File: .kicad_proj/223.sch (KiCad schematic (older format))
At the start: 5 parts, among them U1 ATmega328-PU

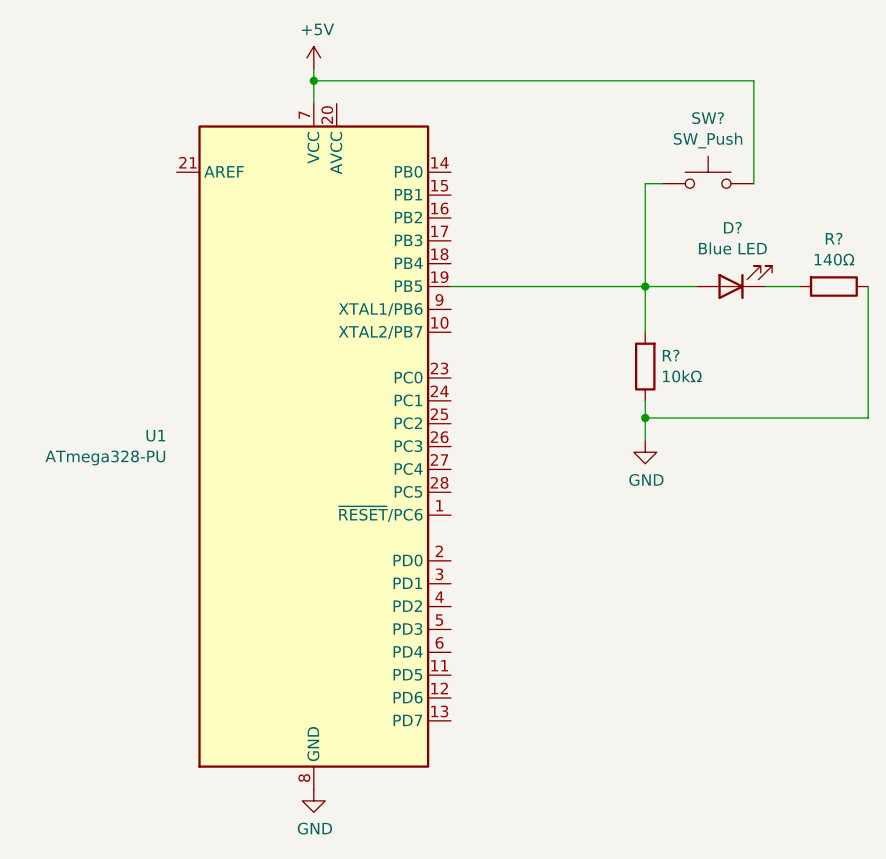
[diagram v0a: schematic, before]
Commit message: Finish 2.2.3, change R values in 2.2.7, change 3-state switch component in 2.2.2
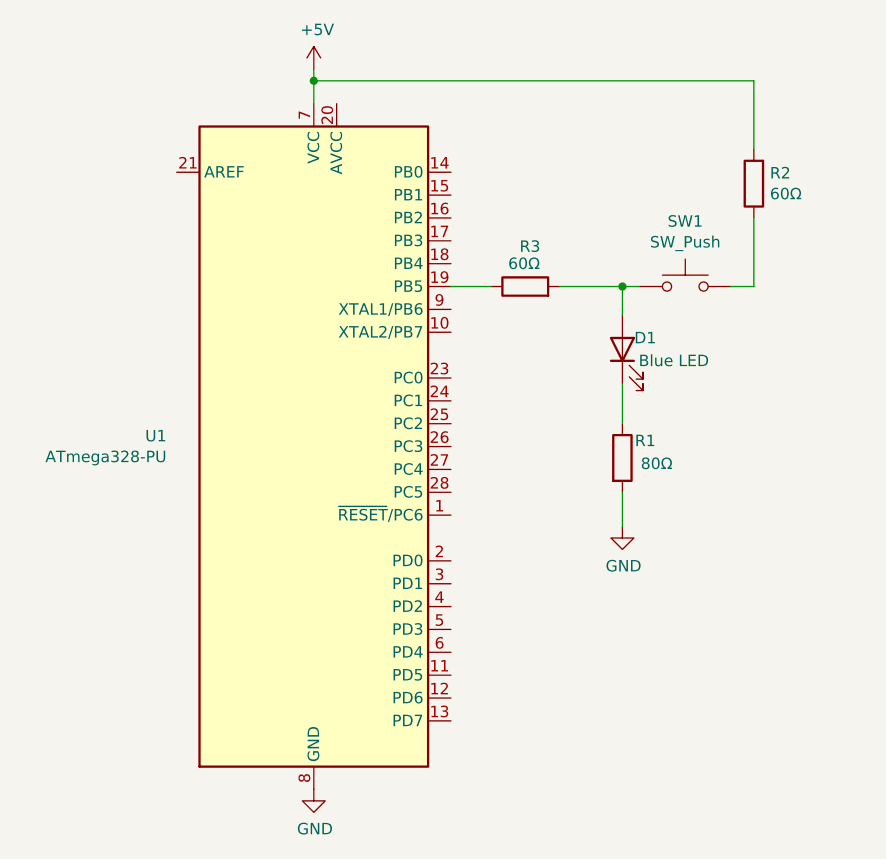
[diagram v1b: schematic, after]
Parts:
- added R3: 60Ω, symbol Device:R
- R1: renamed from R?; value 140Ω -> 80Ω
- R2: renamed from R?; value 10kΩ -> 60Ω
- gave numbers to parts that had none: 2
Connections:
- net +5V: now also R2.2; no longer SW1.2
- net GND: now also R1.2; no longer R1.1, R2.1
- net at D1.2 (A), SW1.1: now also R3.2; no longer R2.2, U1.19 (PB5)
- net at D1.1 (K): now also R1.1; no longer R1.2
- new net: R3.1, U1.19 (PB5)
- new net: R2.1, SW1.2
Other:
- moved on the sheet: D1, R1, R2, SW1
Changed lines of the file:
@@
 L Device:R R?
 U 1 1 607CCF46
-P 6850 3075
+P 5925 3825
 AR Path="/607CCF46" Ref="R?"  Part="1"
-AR Path="/607B21AE/607CCF46" Ref="R?"  Part="1"
-F 0 "R?" V 6643 3075 50  0000 C CNN
-F 1 "140Ω" V 6734 3075 50  0000 C CNN
-F 2 "" V 6780 3075 50  0001 C CNN
-F 3 "~" H 6850 3075 50  0001 C CNN
-	1    6850 3075
-	0    1    1    0
+AR Path="/607B21AE/607CCF46" Ref="R1"  Part="1"
+F 0 "R1" H 6025 3900 50  0000 C CNN
+F 1 "80Ω" H 6075 3800 50  0000 C CNN
+F 2 "" V 5855 3825 50  0001 C CNN
+F 3 "~" H 5925 3825 50  0001 C CNN
+	1    5925 3825
+	1    0    0    -1
 $EndComp
 $Comp
 L Device:LED D?
 U 1 1 607CCF4C
-P 6400 3075
+P 5925 3350
 AR Path="/607CCF4C" Ref="D?"  Part="1"
-AR Path="/607B21AE/607CCF4C" Ref="D?"  Part="1"
-F 0 "D?" H 6393 2820 50  0000 C CNN
-F 1 "Blue LED" H 6393 2911 50  0000 C CNN
-F 2 "" H 6400 3075 50  0001 C CNN
-F 3 "~" H 6400 3075 50  0001 C CNN
-	1    6400 3075
-	-1   0    0    1
+AR Path="/607B21AE/607CCF4C" Ref="D1"  Part="1"
+F 0 "D1" V 5975 3250 50  0000 C CNN
+F 1 "Blue LED" V 5875 3125 50  0000 C CNN
+F 2 "" H 5925 3350 50  0001 C CNN
+F 3 "~" H 5925 3350 50  0001 C CNN
+	1    5925 3350
+	0    -1   -1   0
 $EndComp
 $Comp
 L power:GND #PWR?
 U 1 1 607CCF52
-P 6025 3750
+P 5925 4125
 AR Path="/607CCF52" Ref="#PWR?"  Part="1"
 AR Path="/607B21AE/607CCF52" Ref="#PWR?"  Part="1"
-F 0 "#PWR?" H 6025 3500 50  0001 C CNN
-F 1 "GND" H 6030 3577 50  0000 C CNN
-F 2 "" H 6025 3750 50  0001 C CNN
-F 3 "" H 6025 3750 50  0001 C CNN
-	1    6025 3750
+F 0 "#PWR?" H 5925 3875 50  0001 C CNN
+F 1 "GND" H 5930 3952 50  0000 C CNN
+F 2 "" H 5925 4125 50  0001 C CNN
+F 3 "" H 5925 4125 50  0001 C CNN
+	1    5925 4125
 	1    0    0    -1
 $EndComp
@@
 L Switch:SW_Push SW?
 U 1 1 607CCF58
-P 6300 2625
+P 6200 3075
 AR Path="/607CCF58" Ref="SW?"  Part="1"
-AR Path="/607B21AE/607CCF58" Ref="SW?"  Part="1"
-F 0 "SW?" H 6300 2910 50  0000 C CNN
-F 1 "SW_Push" H 6300 2819 50  0000 C CNN
-F 2 "" H 6300 2825 50  0001 C CNN
-F 3 "~" H 6300 2825 50  0001 C CNN
-	1    6300 2625
+AR Path="/607B21AE/607CCF58" Ref="SW1"  Part="1"
+F 0 "SW1" H 6200 3360 50  0000 C CNN
+F 1 "SW_Push" H 6200 3269 50  0000 C CNN
+F 2 "" H 6200 3275 50  0001 C CNN
+F 3 "~" H 6200 3275 50  0001 C CNN
+	1    6200 3075
 	1    0    0    -1
 $EndComp
@@
 	4575 2175 6500 2175
 Wire Wire Line
-	6500 2175 6500 2625
+	6500 2175 6500 2475
 Connection ~ 4575 2175
 Wire Wire Line
 	4575 2175 4575 2275
-Wire Wire Line
-	6100 2625 6025 2625
 $Comp
 L Device:R R?
 U 1 1 607CCF63
-P 6025 3425
+P 6500 2625
 AR Path="/607CCF63" Ref="R?"  Part="1"
-AR Path="/607B21AE/607CCF63" Ref="R?"  Part="1"
-F 0 "R?" H 5955 3379 50  0000 R CNN
-F 1 "10kΩ" H 5955 3470 50  0000 R CNN
-F 2 "" V 5955 3425 50  0001 C CNN
-F 3 "~" H 6025 3425 50  0001 C CNN
-	1    6025 3425
+AR Path="/607B21AE/607CCF63" Ref="R2"  Part="1"
+F 0 "R2" H 6430 2579 50  0000 R CNN
+F 1 "60Ω" H 6430 2670 50  0000 R CNN
+F 2 "" V 6430 2625 50  0001 C CNN
+F 3 "~" H 6500 2625 50  0001 C CNN
+	1    6500 2625
 	-1   0    0    1
 $EndComp
 Wire Wire Line
-	6025 2625 6025 3075
-Connection ~ 6025 3075
+	5925 3200 5925 3075
 Wire Wire Line
-	6025 3075 6025 3275
+	5925 3500 5925 3675
 Wire Wire Line
-	6025 3575 6025 3650
+	5925 3075 6000 3075
 Wire Wire Line
-	6550 3075 6700 3075
+	6500 2775 6500 3075
 Wire Wire Line
-	7000 3075 7000 3650
+	6500 3075 6400 3075
 Wire Wire Line
-	7000 3650 6025 3650
-Connection ~ 6025 3650
+	5925 3975 5925 4125
+$Comp
+L Device:R R?
+U 1 1 60A3953D
+P 5500 3075
+AR Path="/60A3953D" Ref="R?"  Part="1"
+AR Path="/607B21AE/60A3953D" Ref="R3"  Part="1"
+F 0 "R3" V 5675 3100 50  0000 R CNN
+F 1 "60Ω" V 5600 3150 50  0000 R CNN
+F 2 "" V 5430 3075 50  0001 C CNN
+F 3 "~" H 5500 3075 50  0001 C CNN
+	1    5500 3075
+	0    -1   -1   0
+$EndComp
 Wire Wire Line
-	6025 3650 6025 3750
+	5175 3075 5350 3075
 Wire Wire Line
-	6250 3075 6025 3075
-Wire Wire Line
-	5175 3075 6025 3075
+	5650 3075 5925 3075
+Connection ~ 5925 3075
 $EndSCHEMATC
